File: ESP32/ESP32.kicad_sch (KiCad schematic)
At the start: 39 parts, among them P1 USB_C_Plug_USB2.0, Q1 S8050, U1 ESP32-S3, U2 W25Q128JV, U3 APS1604M-3SQRx-SN, U5 AMS1117, U6 TP4056-42-ESOP8, U7 TPS70402, Y1 Crystal

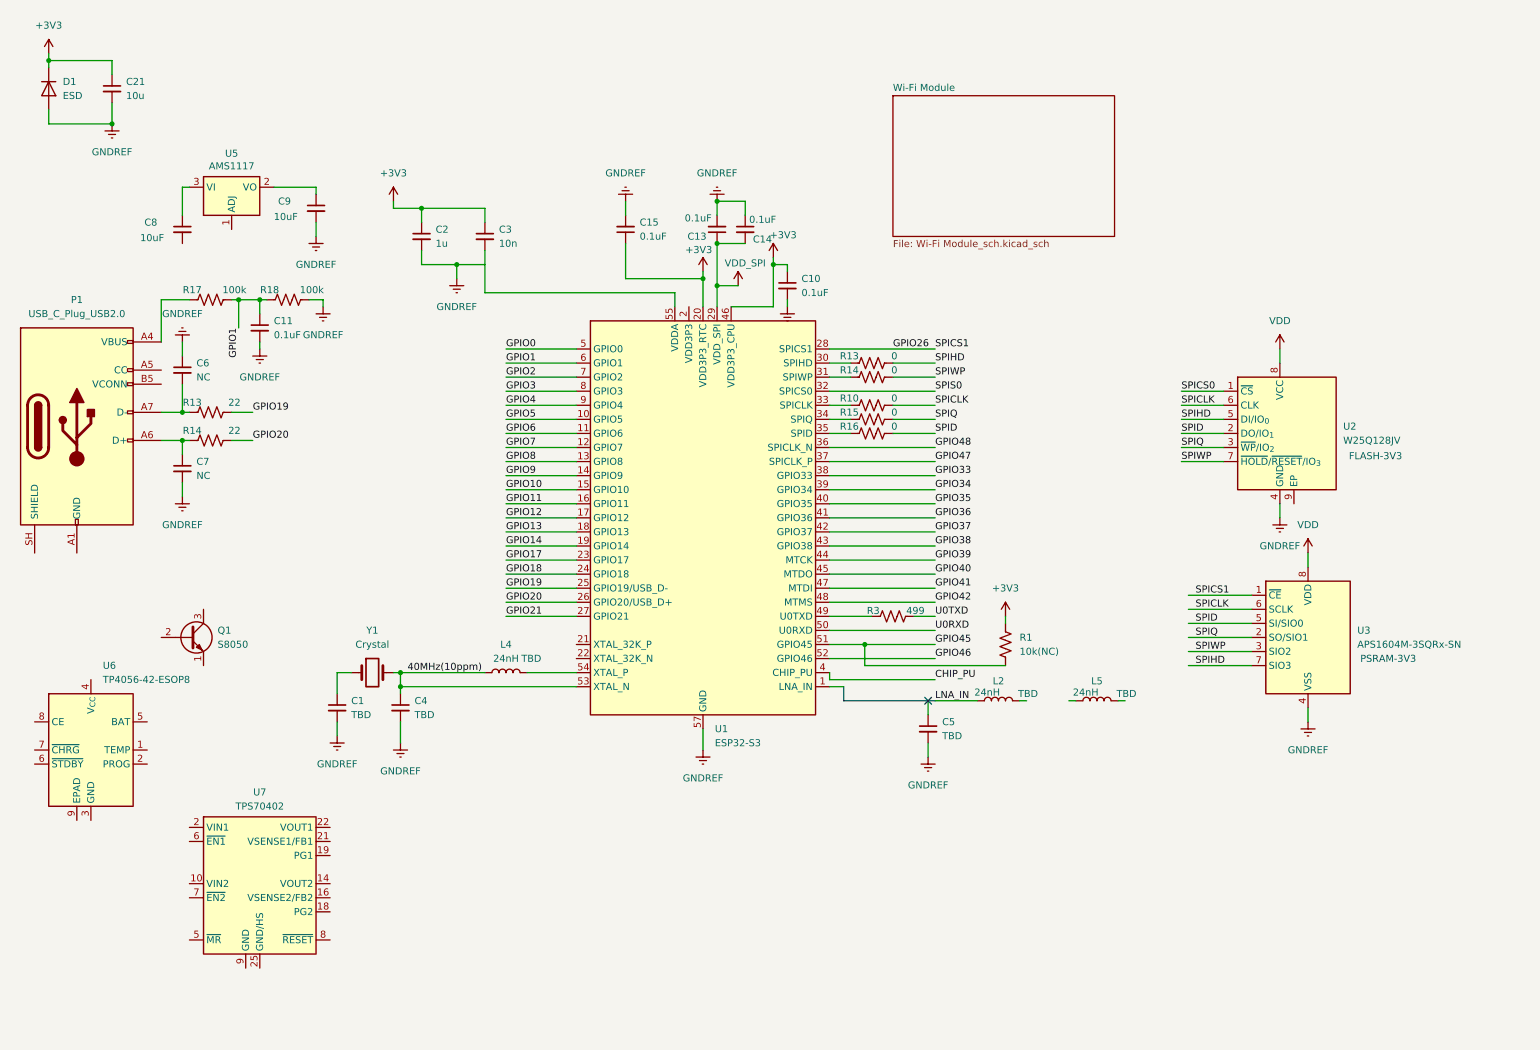
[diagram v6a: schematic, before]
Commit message: ESP32 New Version
V9
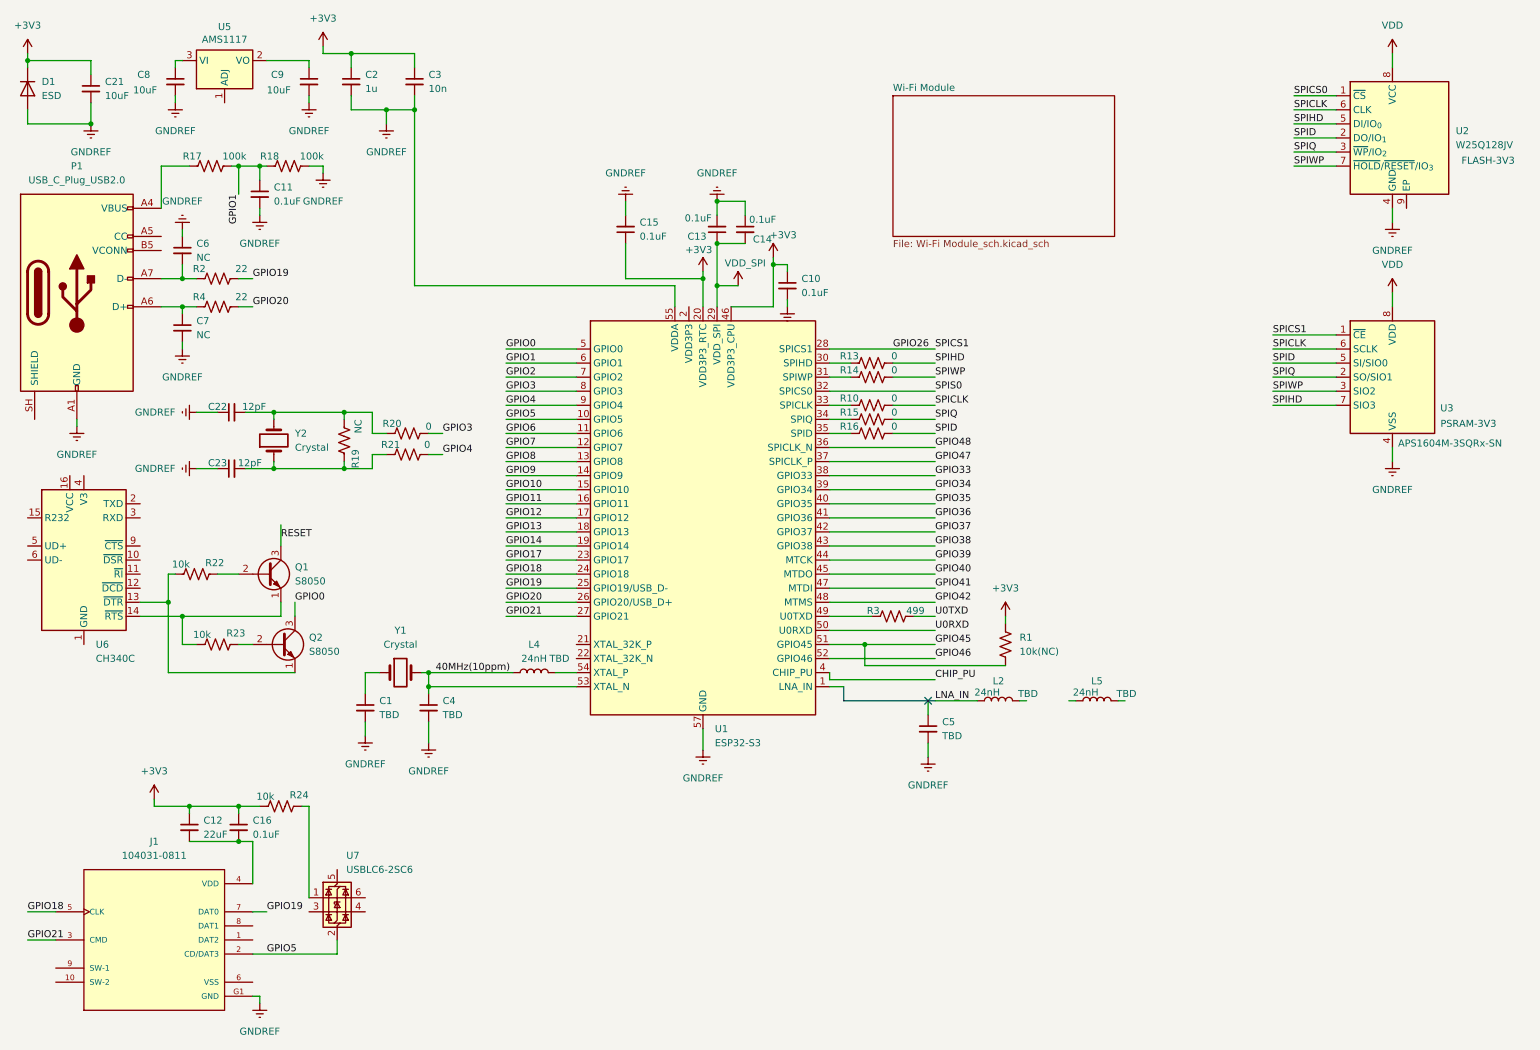
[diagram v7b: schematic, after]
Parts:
- removed U6: TP4056-42-ESOP8, Package_SO:SOIC-8-1EP_3.9x4.9mm_P1.27mm_EP2.41x3.3mm_ThermalVias, symbol Battery_Management:TP4056-42-ESOP8
- removed U7: TPS70402, Package_SO:HTSSOP-24-1EP_4.4x7.8mm_P0.65mm_EP3.4x7.8mm_Mask2.4x4.68mm_ThermalVias, symbol Regulator_Linear:TPS70402
- added C12: 22uF, symbol Device:C_Small
- added C16: 0.1uF, symbol Device:C_Small
- added C22, C23: 12pF, symbol Device:C_Small
- added J1: 104031-0811, 104031-0811:MOLEX_104031-0811, symbol ESP32_sym:104031-0811
- added Q2: S8050, Package_TO_SOT_THT:TO-92_Inline, symbol Transistor_BJT:S8050
- added R19: NC, symbol Device:R_US
- added R20, R21: 0, symbol Device:R_US
- added R22, R23, R24: 10k, symbol Device:R_US
- added U6: CH340C, Package_SO:SOIC-16_3.9x9.9mm_P1.27mm, symbol Interface_USB:CH340C
- added U7: USBLC6-2SC6, Package_TO_SOT_SMD:SOT-23-6, symbol Power_Protection:USBLC6-2SC6
- added Y2: Crystal, symbol Device:Crystal
- C21: value 10u -> 10uF
- renumbered R13 to R2, R14 to R4
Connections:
- net GNDREF is gone; now on net GND: C1.2, C10.2, C11.2, C13.2, C14.1, C15.2, C2.2, C21.2, C4.2, C5.2, C6.1, C7.2, C9.2, D1.2 (A), R18.2, U1.57 (GND), U2.4 (GND), U3.4 (VSS)
- net +3V3: now also C12.1, C16.1, R24.2
- net GPIO0: now also Q2.3 (C)
- net GPIO18: now also J1.5 (CLK)
- net GPIO19: now also J1.7 (DAT0)
- net GPIO21: now also J1.3 (CMD)
- net GPIO3: now also R20.1
- net GPIO4: now also R21.1
- net GPIO5: now also J1.2 (CD/DAT3), U7.2 (GND)
- net at Q1.1 (E): now also R23.2, U6.14 (~{RTS})
- net at Q1.2 (B): now also R22.1
- net RESET: now reaches Q1.3 (C)
- net GND: now reaches P1.A1 (GND), P1.A12 (GND), P1.B1 (GND), P1.B12 (GND)
- net GND: now also C3.2, C8.2, U1.55 (VDDA), U1.56 (VDDA), C22.1, C23.1, J1.G1 (GND), J1.G2 (GND), J1.G3 (GND), J1.G4 (GND)
- new net: Q2.1 (E), R22.2, U6.13 (~{DTR})
- new net: Q2.2 (B), R23.1
- new net: C12.2, C16.2, J1.4 (VDD)
- new net: C23.2, R19.1, R21.2, Y2.1
- new net: C22.2, R19.2, R20.2, Y2.2
- new net: R24.1, U7.1 (I/O1)
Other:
- moved on the sheet: C1, C11, C2, C21, C3, C4, C6, C7, C8, C9, D1, L4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

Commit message: Update the CH340C
Revise the CH340C this materials
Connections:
- net RESET is gone; now on net CHIP_PU: Q1.3 (C)
- net +3V3: now also U6.16 (VCC)
- net GND: now also U6.1 (GND)
- net U0RXD: now also U6.2 (TXD)
- net U0TXD: now also U6.3 (RXD)
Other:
- moved on the sheet: Q1, Q2, R22, R23, U6
